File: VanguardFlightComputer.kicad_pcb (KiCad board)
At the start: 4 copper layers, 56 x 32 mm, 56 parts, among them IC1 ST1L05CPU33R, IC2 ASM330LHHTR, IC3 MAX-M10S-00B, J1 USB_C_Receptacle, J2 MEM2067-02-180-00-A, J3 Conn_Coaxial, U1 STM32H743VGTx, U2 LD1117S50TR_SOT223, U3 USBLC6-2P6, U4 LSM303C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

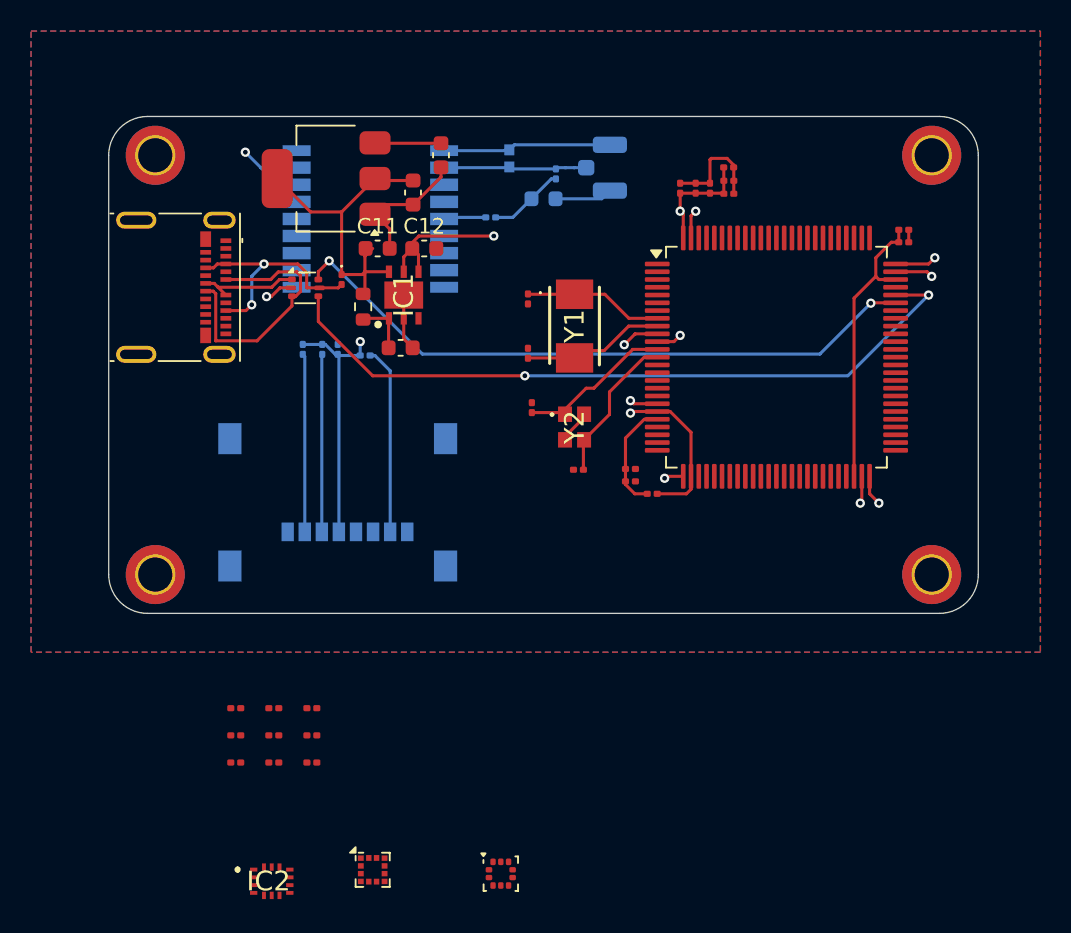
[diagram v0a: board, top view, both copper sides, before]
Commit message: Added all sensors and telemetry modem
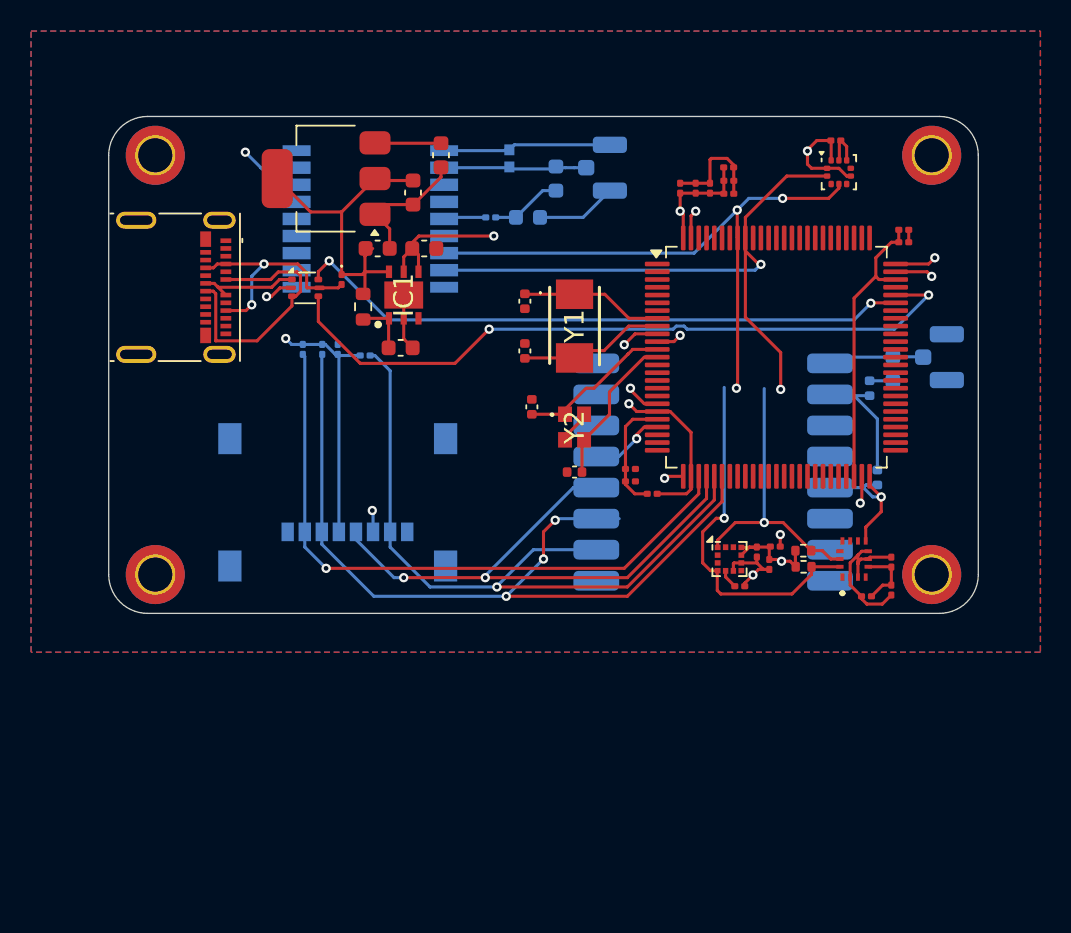
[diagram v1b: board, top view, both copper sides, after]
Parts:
- added C38: 10uF, Capacitor_SMD:C_0402_1005Metric, B.Cu at (139.5, 98.8)
- added C39: 10nF, Capacitor_SMD:C_0402_1005Metric, B.Cu at (139.0, 93.0)
- added FB3: 1k 100MHz, Capacitor_SMD:C_0603_1608Metric, B.Cu at (140.5, 91.8)
- added J4: Conn_Coaxial, Connector_Coaxial:U.FL_Hirose_U.FL-R-SMT-1_Vertical, B.Cu at (143.5, 91.0)
- added R3: 10k, Resistor_SMD:R_0402_1005Metric, F.Cu at (134.7, 103.5)
- added U7: RFM95W-915S2, RF_Module:HOPERF_RFM9XW_SMD, B.Cu at (128.9, 98.4)
- C16, C17, C18, C19: footprint Capacitor_SMD:C_0201_0603Metric -> Capacitor_SMD:C_0402_1005Metric
- FB2: footprint Capacitor_SMD:C_0201_0603Metric -> Capacitor_SMD:C_0603_1608Metric
- R2: footprint Resistor_SMD:R_0201_0603Metric -> Resistor_SMD:R_0402_1005Metric
- moved C27 51.0 mm to (136.8, 77.0)
- moved U5 50.1 mm to (137.0, 79.1)
- moved C20 43.3 mm to (140.4, 104.2), turned to 90 degrees
- moved C21 43.2 mm to (140.4, 106.0), turned to -90 degrees
- moved IC2 42.9 mm to (138.0, 104.0), turned to 90 degrees
- moved C22 42.0 mm to (138.8, 106.4), turned to 180 degrees
- moved C24 34.5 mm to (132.9, 103.2)
- moved C25 34.4 mm to (132.5, 104.3), turned to -90 degrees
- moved R2 34.1 mm to (134.8, 104.5)
- moved C23 31.0 mm to (130.6, 105.8)
- moved U4 30.5 mm to (130.0, 104.0)
- moved C26 30.4 mm to (131.7, 103.5), turned to -90 degrees
- moved C29 1.56 mm to (117.0, 82.0)
- moved FB2 0.30 mm to (118.8, 79.5)
- moved C19 0.29 mm to (120.0, 98.4)
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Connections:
- J2 pad P2: SPI1_CS -> SD_CS
- R4 pad 2: SPI1_CS -> SD_CS
- U1 pad 22: unconnected-(U1-PA0-Pad22) -> TELEM_CS
- U1 pad 28: unconnected-(U1-PA4-Pad28) -> SD_CS
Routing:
- net I2C1_SDA: track 0.00 -> 62.6 mm, vias 0 -> 4
- net I2C1_SCL: track 0.00 -> 59.5 mm, vias 0 -> 3
- net SPI1_MOSI: track 11.4 -> 53.9 mm, vias 0 -> 3
- net SD_CS: track 0.00 -> 41.5 mm, vias 0 -> 1
- net SPI1_SCK: track 0.00 -> 37.3 mm, vias 0 -> 2
- net SPI1_MISO: track 12.1 -> 46.3 mm, vias 0 -> 1
- net GND: track 50.0 -> 82.1 mm, vias 7 -> 10
- net +3.3V: track 56.3 -> 78.2 mm, vias 8 -> 10
- net SPI1_CS: track 11.5 -> 0.00 mm
- net Net-(J4-In): track 0.00 -> 6.19 mm
- net TELEM_CS: track 0.00 -> 4.86 mm, vias 0 -> 1
- net Net-(IC2-VDDIO): track 0.00 -> 4.23 mm
- net USB_DM: track 41.8 -> 40.0 mm
- net Net-(C39-Pad1): track 0.00 -> 1.50 mm
- net Net-(U4-C1): track 0.00 -> 1.23 mm
